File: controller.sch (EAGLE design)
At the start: 45 parts, among them IC1 7805DT, Q3 MOSFET-NCHANNELFDD8780, Q5 MMBT4403, SW1 ROTARTY_ENCODER, U1 ATMEGA328P, Y1 16MHz

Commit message: controller board layout complete.
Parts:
- removed D6: WHITE, SparkFun-LED:LED-WHITE
- removed S1: (no value), SparkFun-Electromechanical:SWITCH-SPDTPTH3
- added Q2: MOSFET-NCHANNELBSS123LT1G, SparkFun-DiscreteSemi:MOSFET-NCHANNELBSS123LT1G
- added U$13: SWITCH-SPDT, jt_parts:SWITCH-SPDT
- D1, D2, D3, D4, D5: device SparkFun-LED:LED-WHITE -> SparkFun-LED:LED3MM
- SW1: value ROTARTY_ENCODER -> ROT_ENCODER; device SparkFun-Electromechanical:ROTARTY_ENCODER -> jt_parts:ROT_ENCODER
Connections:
- removed net N$8: 12V_IN.2, S1.P
- removed net NIGHT: U$3.1
- new net N$12: D1.C, D2.C, D3.C, D4.C, D5.C, Q2.D
- new net NITE: Q2.G, U1.PC0(ADC0)
- net 12V: now also 12V_IN.2, U$13.1, U$13.2, U$13.3; no longer S1.O, S1.S
- net 5V: now also JP1.6, JP2.VCC, U$12.2, U$3.1
- net GND: now also Q2.S, SW1.C; no longer D1.C, D2.C, D3.C, D4.C, D5.C, D6.C
- net N$9: no longer D6.A
- net VCC: no longer JP1.6, JP2.VCC, U$12.2
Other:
- note removed: "ADD MOSFET"
- moved on the sheet: 12V_IN, C4, C5, C8, D1, D2, D3, D4, D5, LEDSTRIP, Q3, Q4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

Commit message: added fuse. tore up power traces.
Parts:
- added U$15: FUSE, jt_parts:FUSE
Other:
- note removed: "MAKE FOOTPRINT"
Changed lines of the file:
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@@
 <setting verticaltext="up"/>
 </settings>
-<grid distance="0.05" unitdist="inch" unit="inch" style="lines" multiple="1" display="no" altdistance="0.01" altunitdist="inch" altunit="inch"/>
+<grid distance="0.1" unitdist="inch" unit="inch" style="lines" multiple="1" display="no" altdistance="0.01" altunitdist="inch" altunit="inch"/>
 <layers>
 <layer number="1" name="Top" color="4" fill="1" visible="no" active="no"/>
@@
 <part name="GND18" library="SparkFun-Aesthetics" deviceset="GND" device=""/>
 <part name="U$13" library="jt_parts" deviceset="SWITCH-SPDT" device=""/>
+<part name="U$15" library="jt_parts" deviceset="FUSE" device=""/>
 </parts>
 <sheets>
 <sheet>
 <plain>
-<text x="144.78" y="160.02" size="6.4516" layer="91">MAKE FOOTPRINT</text>
 </plain>
 <instances>
@@
 <instance part="GND18" gate="1" x="148.59" y="215.9" rot="R90"/>
 <instance part="U$13" gate="G$1" x="180.34" y="152.4"/>
+<instance part="U$15" gate="G$1" x="170.18" y="165.1"/>
 </instances>
 <busses>

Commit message: commit prior to adding reverse polarity protection.
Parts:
- added U$16: (no value), jt_parts:RESISTOR
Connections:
- net GND: now also U$16.1
- net PWM: now also U$16.2
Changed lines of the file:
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@@
 <setting verticaltext="up"/>
 </settings>
-<grid distance="0.1" unitdist="inch" unit="inch" style="lines" multiple="1" display="no" altdistance="0.01" altunitdist="inch" altunit="inch"/>
+<grid distance="0.05" unitdist="inch" unit="mil" style="lines" multiple="1" display="no" altdistance="0.01" altunitdist="inch" altunit="mil"/>
 <layers>
 <layer number="1" name="Top" color="4" fill="1" visible="no" active="no"/>
@@
 <part name="U$13" library="jt_parts" deviceset="SWITCH-SPDT" device=""/>
 <part name="U$15" library="jt_parts" deviceset="FUSE" device=""/>
+<part name="U$16" library="jt_parts" deviceset="RESISTOR" device=""/>
+<part name="GND19" library="SparkFun-Aesthetics" deviceset="GND" device=""/>
 </parts>
 <sheets>
@@
 <instance part="U$13" gate="G$1" x="180.34" y="152.4"/>
 <instance part="U$15" gate="G$1" x="170.18" y="165.1"/>
+<instance part="U$16" gate="G$1" x="241.3" y="215.9" smashed="yes" rot="R270">
+<attribute name="VALUE" x="237.998" y="219.71" size="1.778" layer="96" rot="R270"/>
+</instance>
+<instance part="GND19" gate="1" x="241.3" y="226.06" rot="R180"/>
 </instances>
 <busses>
@@
 <wire x1="170.18" y1="149.86" x2="167.64" y2="149.86" width="0.1524" layer="91"/>
 </segment>
+<segment>
+<pinref part="GND19" gate="1" pin="GND"/>
+<pinref part="U$16" gate="G$1" pin="1"/>
+<wire x1="241.3" y1="223.52" x2="241.3" y2="220.98" width="0.1524" layer="91"/>
+</segment>
 </net>
 <net name="RCK" class="0">
@@
 <segment>
 <pinref part="U$6" gate="G$1" pin="1"/>
-<wire x1="236.22" y1="208.28" x2="242.57" y2="208.28" width="0.1524" layer="91"/>
-<label x="237.49" y="208.28" size="1.778" layer="95"/>
-</segment>
-<segment>
+<wire x1="236.22" y1="208.28" x2="241.3" y2="208.28" width="0.1524" layer="91"/>
+<label x="245.11" y="208.28" size="1.778" layer="95"/>
+<pinref part="U$16" gate="G$1" pin="2"/>
+<wire x1="241.3" y1="208.28" x2="252.73" y2="208.28" width="0.1524" layer="91"/>
+<wire x1="241.3" y1="210.82" x2="241.3" y2="208.28" width="0.1524" layer="91"/>
+<junction x="241.3" y="208.28"/>
+</segment>
+<segment>

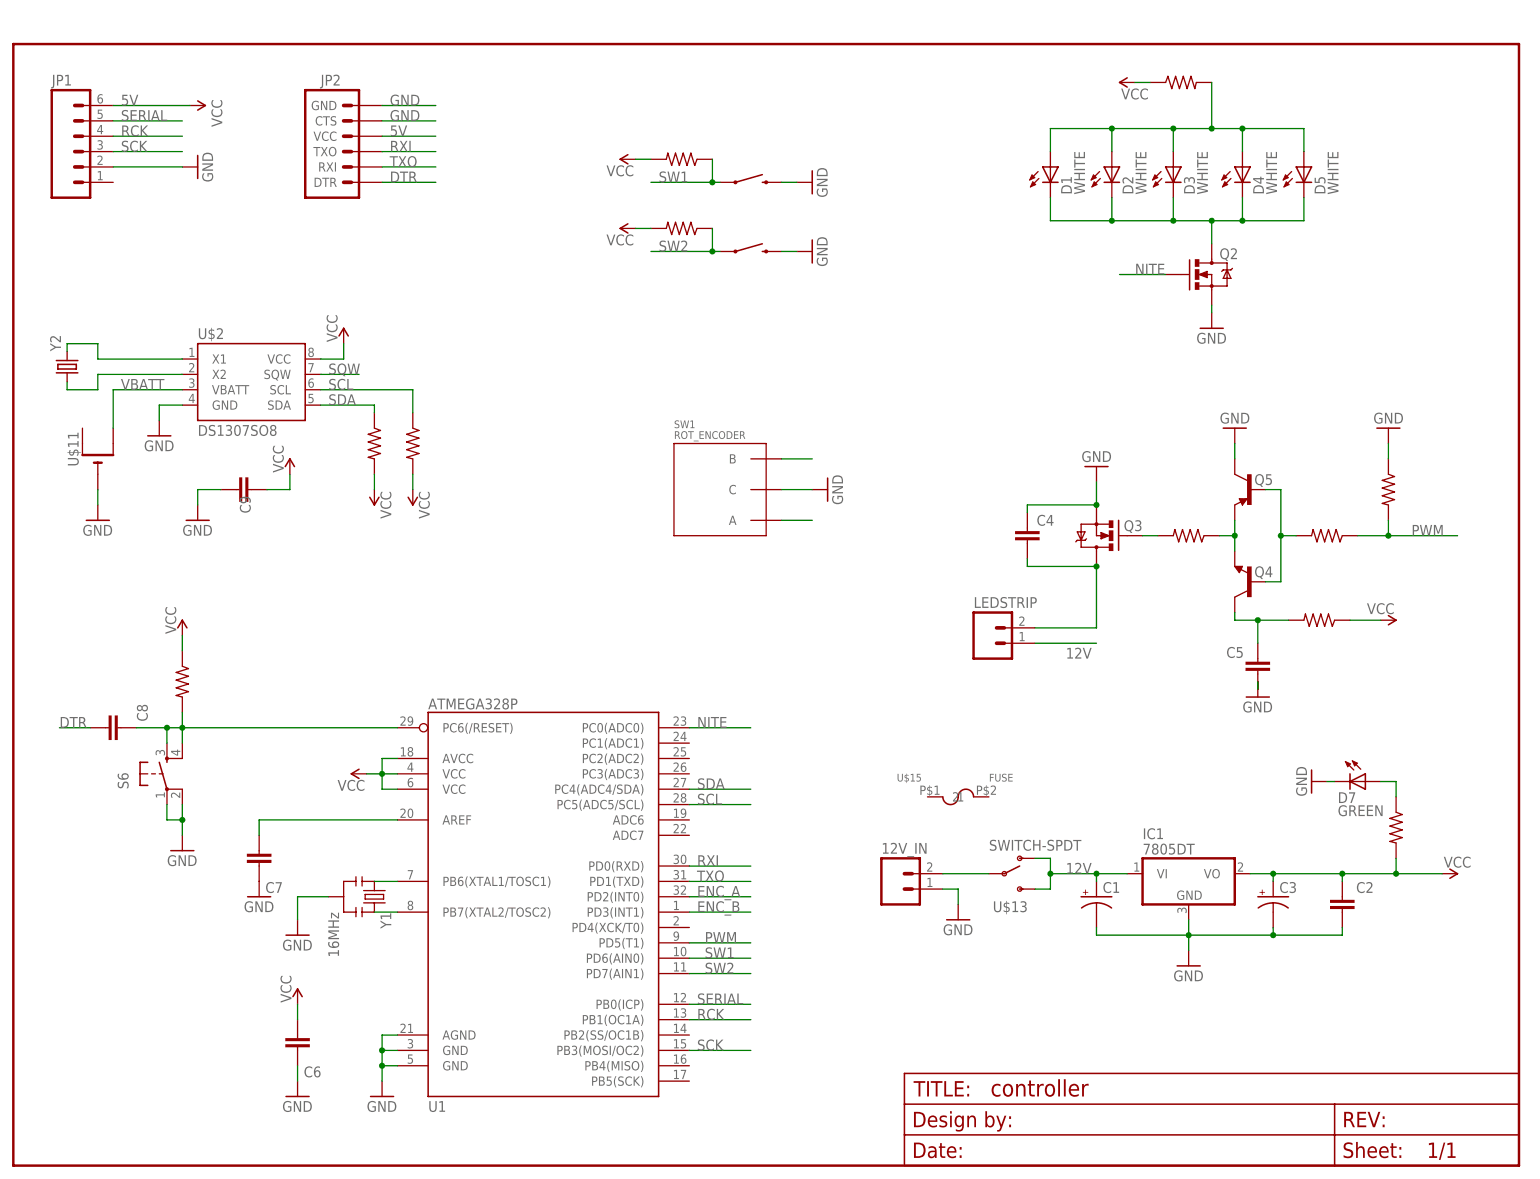
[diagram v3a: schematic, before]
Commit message: began moving controller to smaller board size.
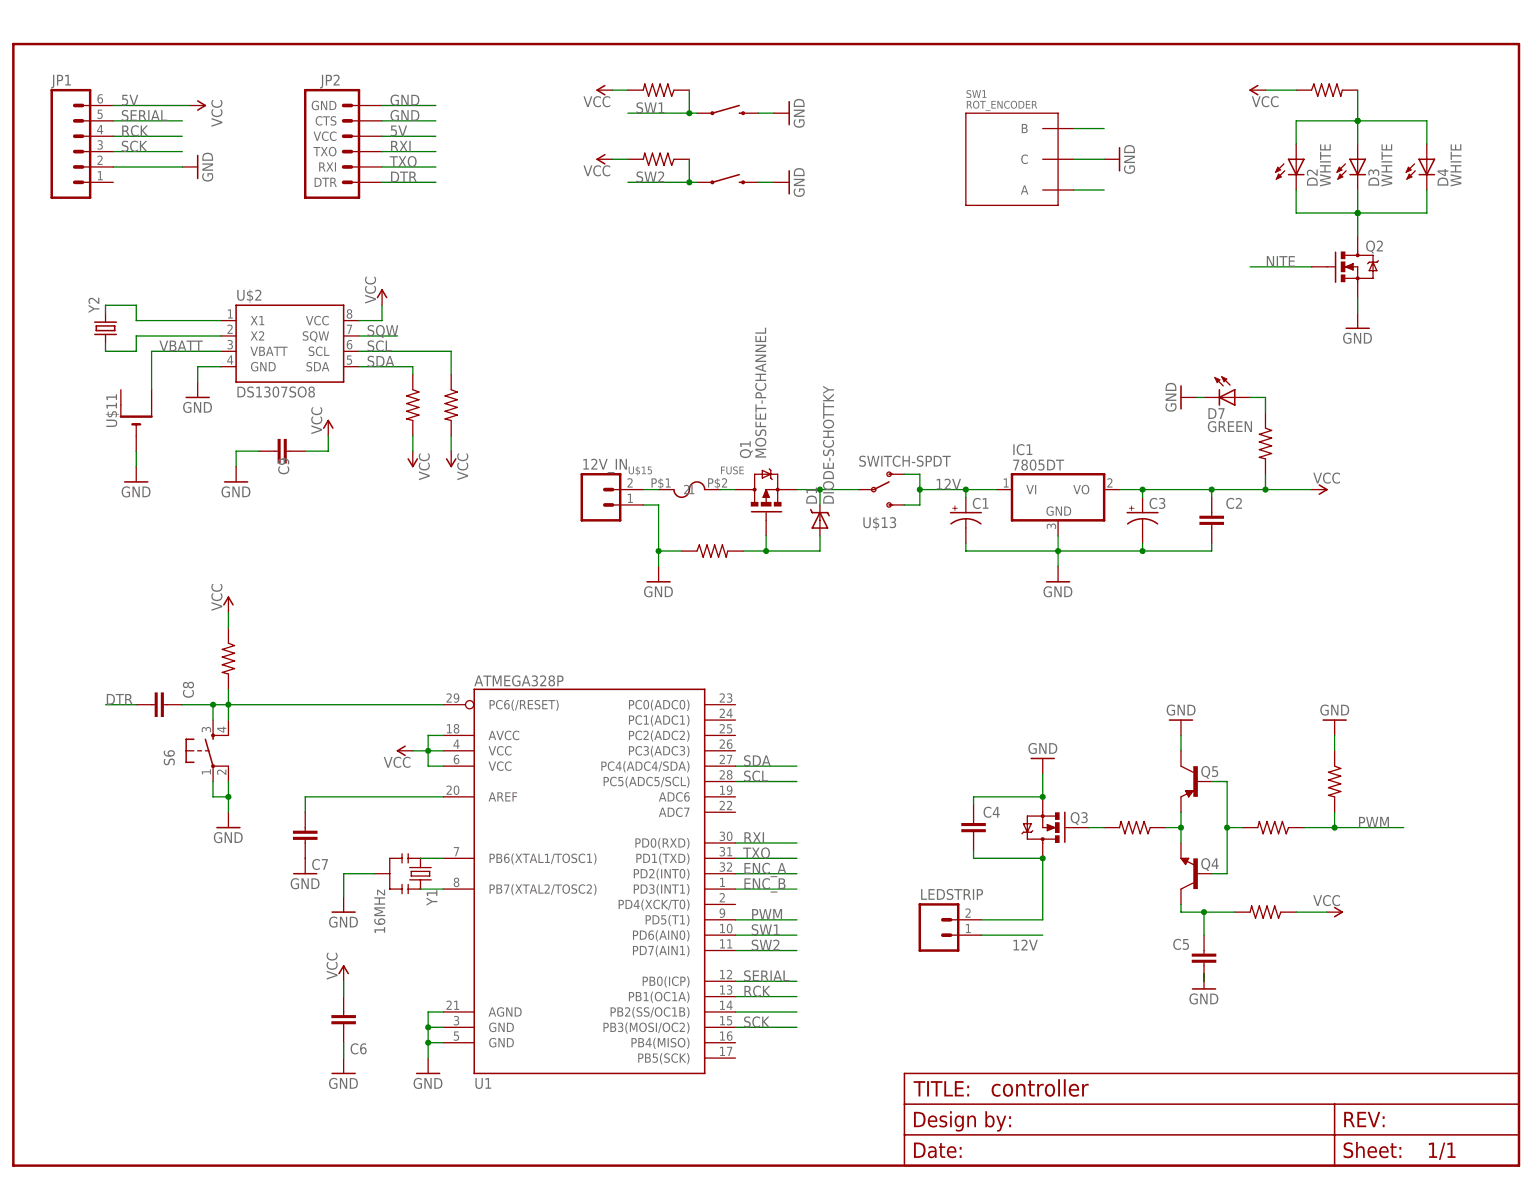
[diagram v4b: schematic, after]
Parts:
- removed D5: WHITE, SparkFun-LED:LED3MM
- added Q1: MOSFET-PCHANNEL, SparkFun-DiscreteSemi:MOSFET-PCHANNEL
- added U$17: (no value), jt_parts:RESISTOR
- D1: value WHITE -> DIODE-SCHOTTKY; device SparkFun-LED:LED3MM -> SparkFun-DiscreteSemi:DIODE-SCHOTTKY
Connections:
- new net N$13: Q1.D, U$15.2
- new net N$14: D1.C, Q1.S, U$13.2
- new net N$16: D1.A, Q1.G, U$17.2
- new net N$8: 12V_IN.2, U$15.1
- net 12V: no longer 12V_IN.2, U$13.2
- net GND: now also U$17.1
- net N$12: no longer D1.C, D5.C
- net N$9: no longer D1.A, D5.A
- net NITE: now also U1.PB2(SS/OC1B); no longer U1.PC0(ADC0)
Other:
- moved on the sheet: 12V_IN, C1, C2, C3, C4, C5, C6, C7, C8, C9, D2, D3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

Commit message: added to do notes to schematic file.
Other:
- note added: "pull down?"
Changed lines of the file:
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@@
 <setting verticaltext="up"/>
 </settings>
-<grid distance="0.05" unitdist="inch" unit="mil" style="lines" multiple="1" display="no" altdistance="0.01" altunitdist="inch" altunit="mil"/>
+<grid distance="0.1" unitdist="inch" unit="inch" style="lines" multiple="1" display="no" altdistance="0.01" altunitdist="inch" altunit="inch"/>
 <layers>
 <layer number="1" name="Top" color="4" fill="1" visible="no" active="no"/>
@@
 <sheet>
 <plain>
+<text x="195.58" y="170.18" size="1.778" layer="91" rot="R90">pull down?</text>
 </plain>
 <instances>

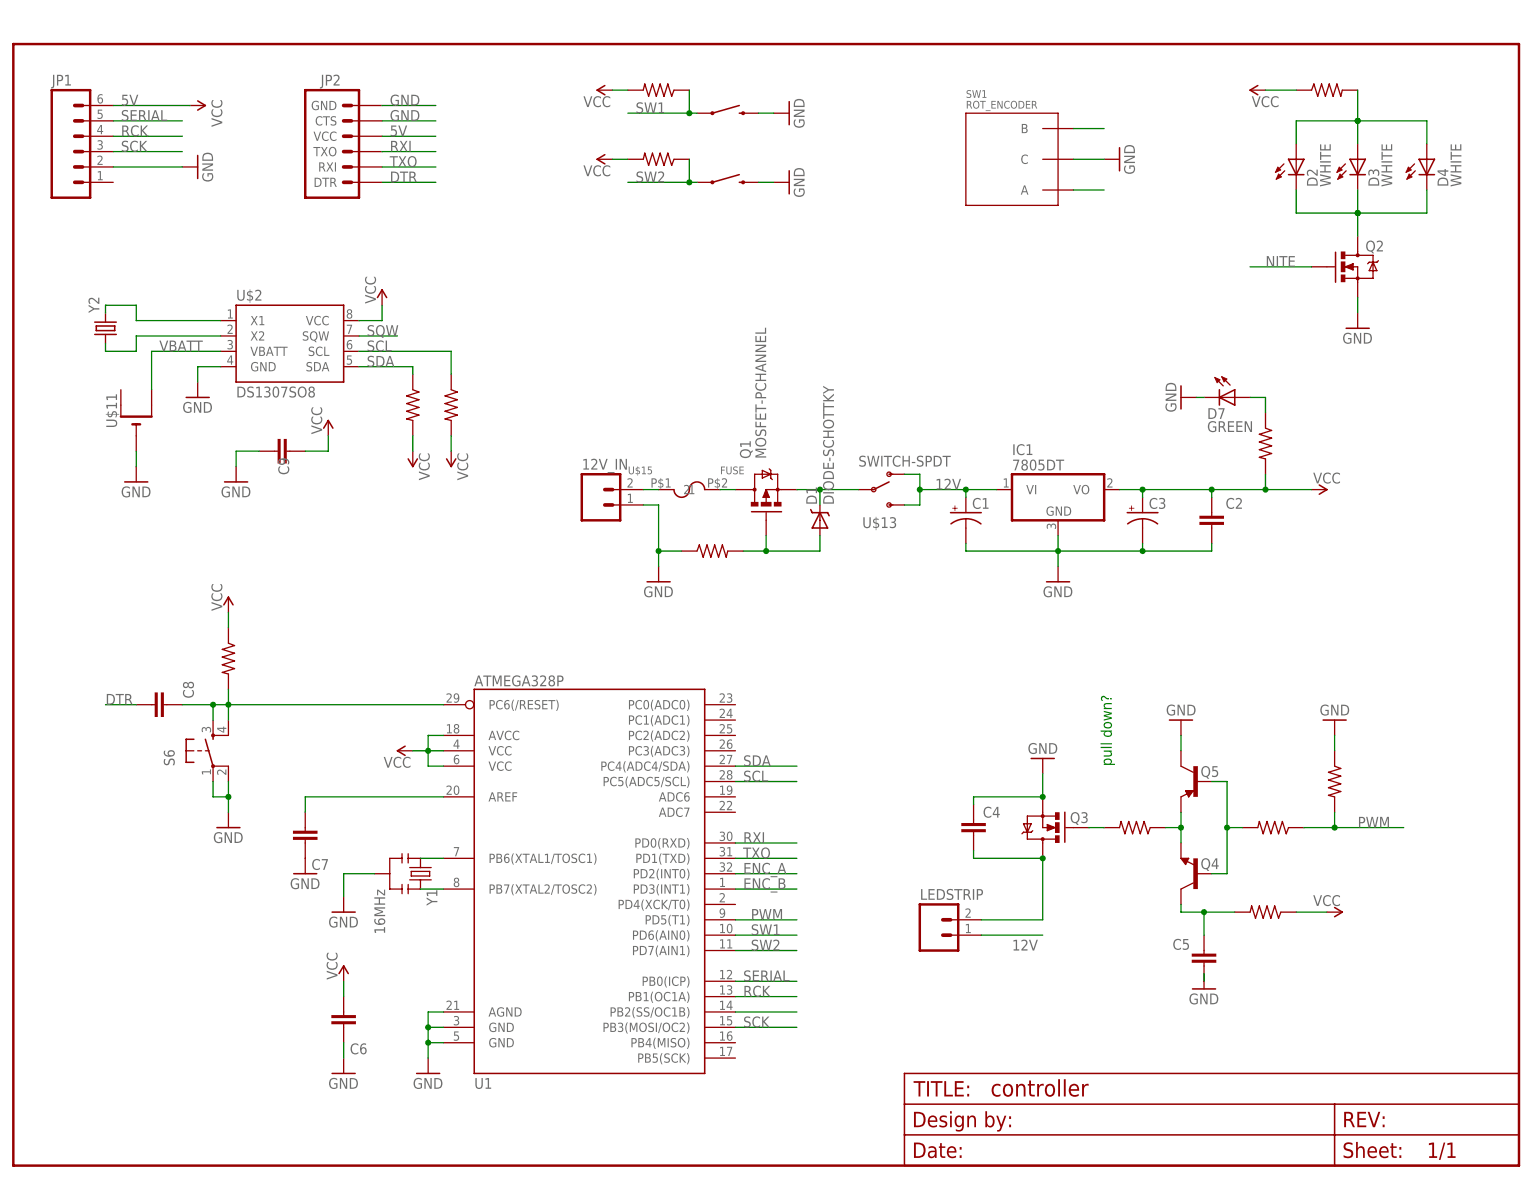
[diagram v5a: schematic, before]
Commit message: removed totem pole, switches, encoder, and disaply board jumper.
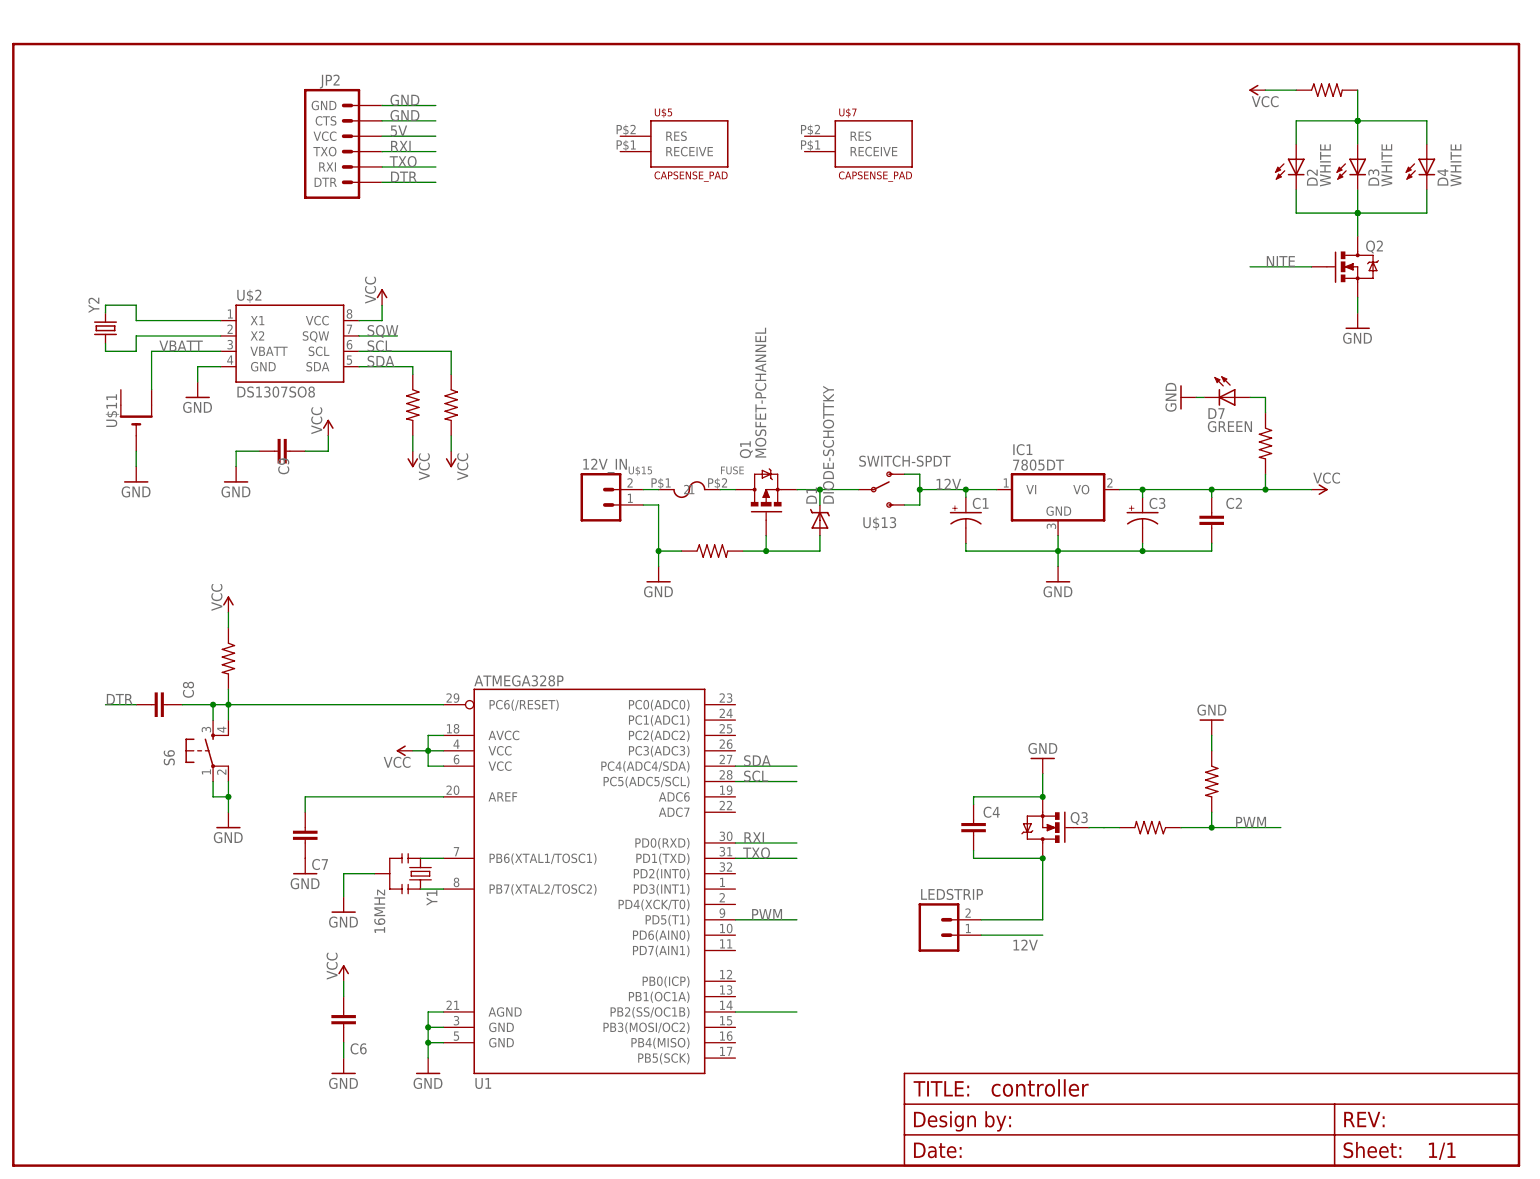
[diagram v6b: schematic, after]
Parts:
- removed C5: (no value), SparkFun-Capacitors:CAP0805
- removed JP1: (no value), SparkFun-Connectors:M06LOCK
- removed Q4: (no value), SparkFun-DiscreteSemi:TRANSISTOR_NPNSOT23
- removed Q5: MMBT4403, SparkFun-DiscreteSemi:TRANSISTOR_PNPMMBT4403
- removed S3, S4: SWITCH-MOMENTARY-2SIDE_EZ, SparkFun-Electromechanical:SWITCH-MOMENTARY-2SIDE_EZ
- removed SW1: ROT_ENCODER, jt_parts:ROT_ENCODER
- removed U$12, U$14: (no value), jt_parts:RESISTOR
- U$5, U$7: value (none) -> CAPSENSE_PAD; device jt_parts:RESISTOR -> SparkFun-Electromechanical:CAPSENSE_PAD
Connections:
- removed net ENC_A: SW1.A, U1.PD2(INT0)
- removed net ENC_B: SW1.B, U1.PD3(INT1)
- removed net N$2: C5.2, Q4.C, U$7.2
- removed net N$5: Q4.E, Q5.E, U$5.1
- removed net RCK: JP1.4, U1.PB1(OC1A)
- removed net SCK: JP1.3, U1.PB3(MOSI/OC2)
- removed net SERIAL: JP1.5, U1.PB0(ICP)
- removed net SW1: S3.1, U$12.1, U1.PD6(AIN0)
- removed net SW2: S4.1, U$14.1, U1.PD7(AIN1)
- removed net VCC: U$7.1
- net 5V: no longer JP1.6, U$12.2, U$14.2
- net GND: no longer C5.1, JP1.2, Q5.C, S3.2, S4.2, SW1.C
- net N$3: no longer U$5.2
- net NONE: no longer Q4.B, Q5.B
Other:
- note removed: "pull down?"
